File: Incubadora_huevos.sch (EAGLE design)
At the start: 53 parts, among them Q1 2N3904, Q2 2N3904, Q3 2N3904, T1 BT138-H, T2 BT138-H, T3 BT138-H, U1 SHT20

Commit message: Terminado ubicacion componentes. inicio ruteo
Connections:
- net LINEA: now also VAC-2.KL; no longer VAC-1.KL
- net NEUTR: now also VAC-1.KL; no longer VAC-2.KL
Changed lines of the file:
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@@
 <setting verticaltext="up"/>
 </settings>
-<grid distance="0.1" unitdist="inch" unit="inch" style="lines" multiple="1" display="yes" altdistance="0.01" altunitdist="inch" altunit="inch"/>
+<grid distance="0.1" unitdist="inch" unit="inch" style="lines" multiple="1" display="no" altdistance="0.01" altunitdist="inch" altunit="inch"/>
 <layers>
 <layer number="1" name="Top" color="4" fill="1" visible="no" active="no"/>
@@
 <net name="LINEA" class="0">
 <segment>
-<pinref part="VAC" gate="-1" pin="KL"/>
-<wire x1="60.96" y1="30.48" x2="63.5" y2="30.48" width="0.1524" layer="91"/>
-<label x="63.5" y="30.48" size="1.778" layer="95" ratio="10" xref="yes"/>
-</segment>
-<segment>
 <pinref part="R5" gate="G$1" pin="2"/>
 <pinref part="T1" gate="G$1" pin="A2"/>
@@
 <label x="147.32" y="114.3" size="1.778" layer="95" ratio="10" xref="yes"/>
 </segment>
-</net>
-<net name="NEUTR" class="0">
 <segment>
 <pinref part="VAC" gate="-2" pin="KL"/>
@@
 <label x="63.5" y="22.86" size="1.778" layer="95" ratio="10" xref="yes"/>
 </segment>
+</net>
+<net name="NEUTR" class="0">
 <segment>
 <pinref part="BOM1" gate="-2" pin="KL"/>
@@
 <wire x1="236.22" y1="78.74" x2="233.68" y2="78.74" width="0.1524" layer="91"/>
 <label x="233.68" y="78.74" size="1.778" layer="95" ratio="10" rot="R180" xref="yes"/>
+</segment>
+<segment>
+<pinref part="VAC" gate="-1" pin="KL"/>
+<wire x1="60.96" y1="30.48" x2="63.5" y2="30.48" width="0.1524" layer="91"/>
+<label x="63.5" y="30.48" size="1.778" layer="95" ratio="10" xref="yes"/>
 </segment>
 </net>
@@
 </sheet>
 </sheets>
+<errors>
+</errors>
 </schematic>
 </drawing>

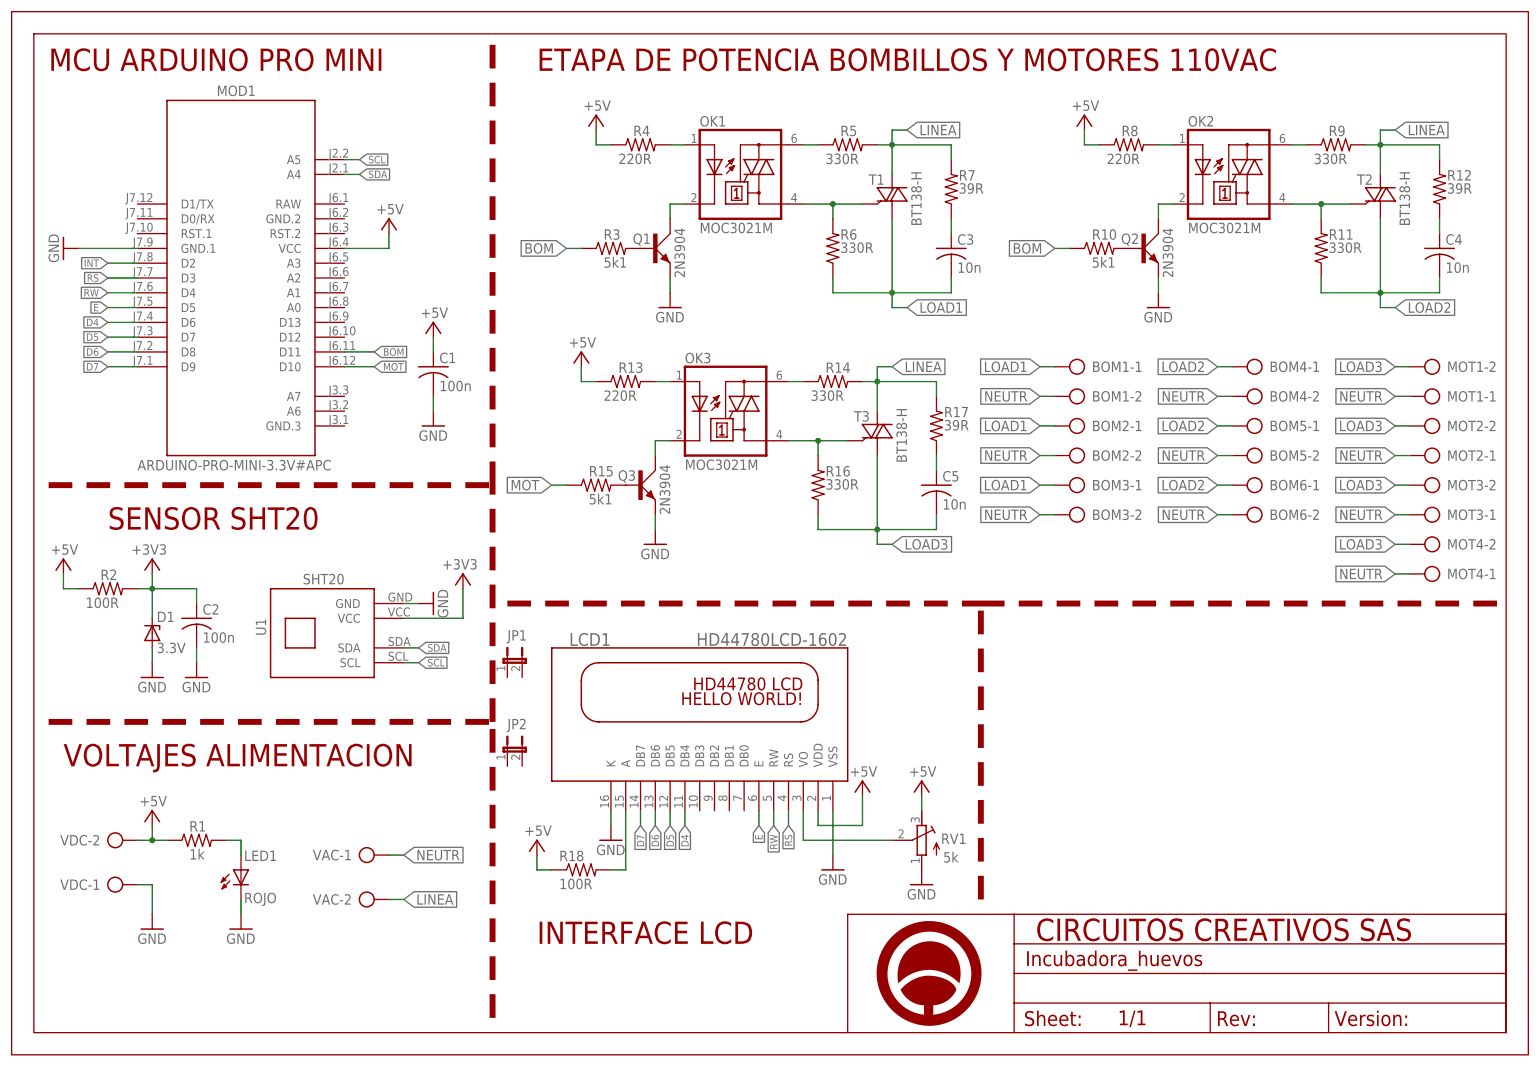
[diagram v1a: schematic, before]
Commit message: Se modifico la etapa de potencia ya que la anterior se calentaba mucho
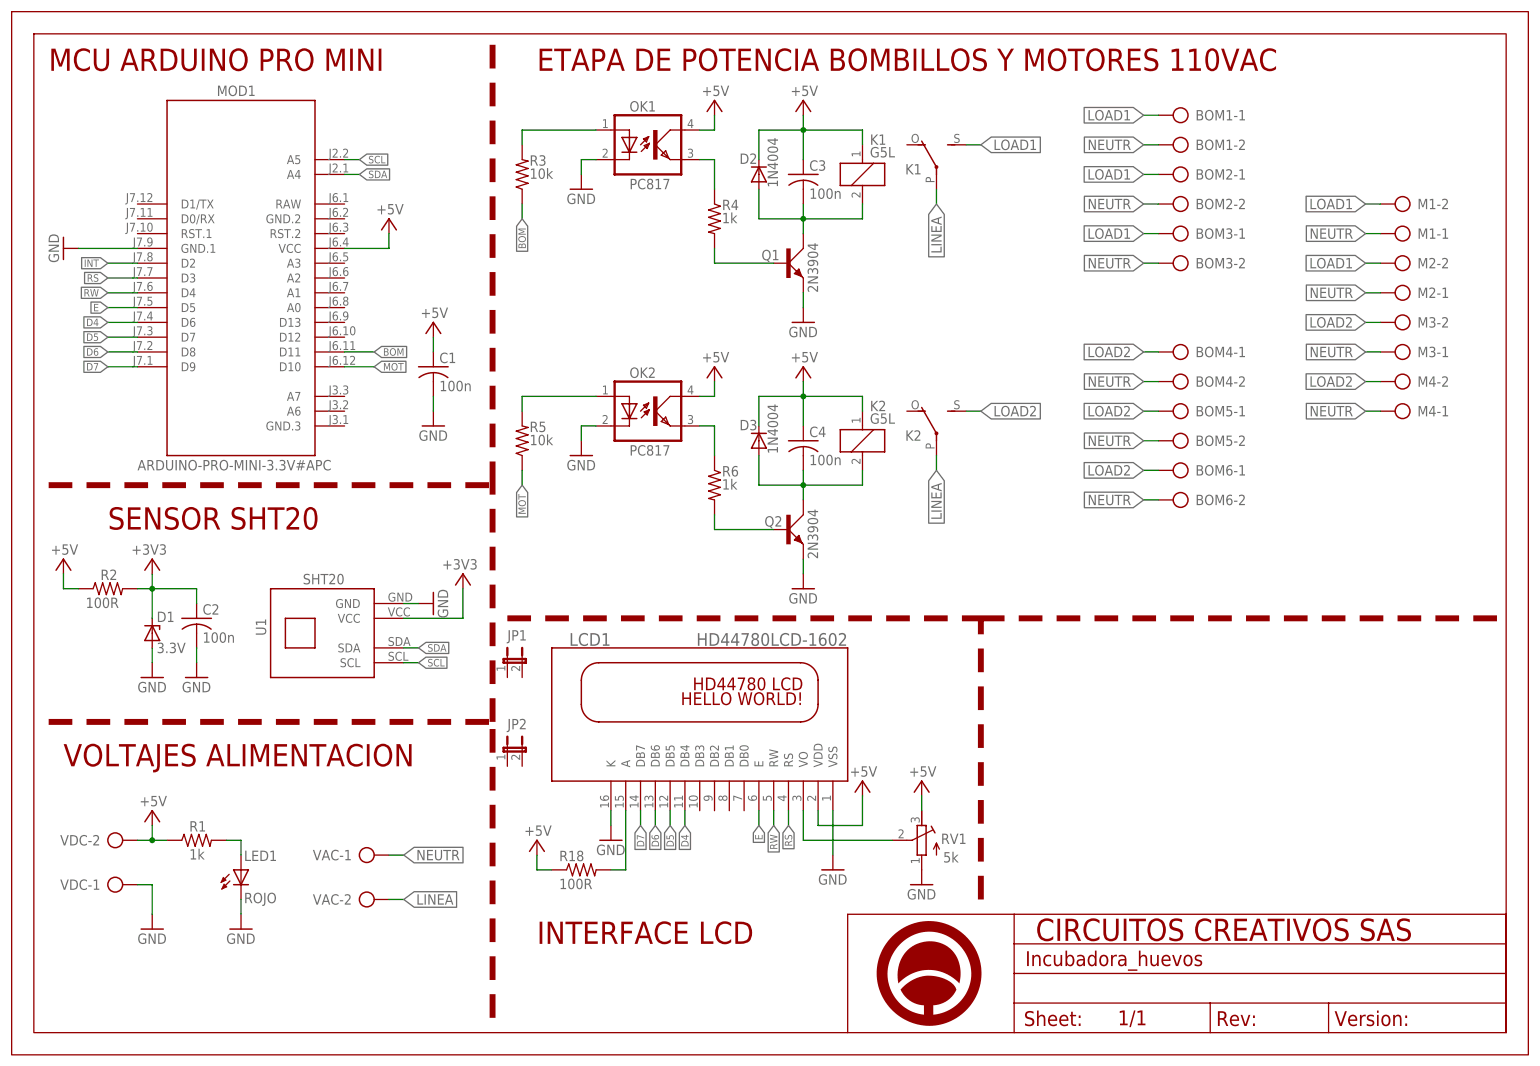
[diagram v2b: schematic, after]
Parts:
- removed C5: 10n, rcl:C-US050-030X075
- removed MOT1, MOT2, MOT3, MOT4: (no value), con-ptr500:AK500/2
- removed OK3: MOC3021M, optocoupler:MOC3021M
- removed Q3: 2N3904, transistor-small-signal:2N3904
- removed R10, R15: 5k1, rcl:R-US_0204/7
- removed R11, R14, R16, R9: 330R, rcl:R-US_0204/7
- removed R12, R17, R7: 39R, rcl:R-US_0204/7
- removed R13, R8: 220R, rcl:R-US_0204/7
- removed T1, T2, T3: BT138-H, triac:BT138-H
- added D2, D3: 1N4004, adafruit:1N4004
- added K1, K2: G5L, relay:G5L
- added M1, M2, M3, M4: (no value), con-ptr500:AK500/2
- C3, C4: value 10n -> 100n; device rcl:C-US050-030X075 -> rcl:C-US025-025X050
- OK1, OK2: value MOC3021M -> PC817; device optocoupler:MOC3021M -> optocoupler:PC817
- R3: value 5k1 -> 10k
- R4: value 220R -> 1k
- R5: value 330R -> 10k
- R6: value 330R -> 1k
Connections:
- removed net LOAD3: C5.2, MOT1-2.KL, MOT2-2.KL, MOT3-2.KL, MOT4-2.KL, R16.1, T3.A1
- removed net N$10: OK2.A2, R9.1
- removed net N$11: Q2.B, R10.2
- removed net N$12: OK2.C, Q2.C
- removed net N$13: C4.1, R12.1
- removed net N$14: OK3.A1, R16.2, T3.G
- removed net N$15: OK3.A, R13.2
- removed net N$16: OK3.A2, R14.1
- removed net N$17: Q3.B, R15.2
- removed net N$18: OK3.C, Q3.C
- removed net N$19: C5.1, R17.1
- removed net N$9: C3.1, R7.1
- new net N$21: C3.2, D2.A, K11.2, Q1.C
- net +5V: now also C3.1, C4.1, D2.C, D3.C, K11.1, K21.1, OK1.COL, OK2.COL; no longer R13.1, R4.1, R8.1
- net BOM: no longer R10.1
- net GND: now also OK1.C, OK2.C; no longer Q3.E
- net LINEA: now also K12.P, K22.P; no longer R12.2, R14.2, R17.2, R5.2, R7.2, R9.2, T1.A2, T2.A2, T3.A2
- net LOAD1: now also K12.S, M1-2.KL, M2-2.KL; no longer C3.2, R6.1, T1.A1
- net LOAD2: now also K22.S, M3-2.KL, M4-2.KL; no longer C4.2, R11.1, T2.A1
- net MOT: now also R5.1; no longer R15.1
- net N$2: now also OK1.EMIT, R4.1; no longer OK1.A1, R6.2, T1.G
- net N$3: now also Q1.B; no longer OK1.A
- net N$4: now also OK1.A, R3.2; no longer OK1.A2, R5.1
- net N$5: now also C4.2, D3.A, K21.2, Q2.C; no longer Q1.B, R3.2
- net N$6: now also OK2.EMIT, R6.1; no longer OK1.C, Q1.C
- net N$7: now also Q2.B, R6.2; no longer OK2.A1, R11.2, T2.G
- net N$8: now also R5.2; no longer R8.2
- net NEUTR: now also M1-1.KL, M2-1.KL, M3-1.KL, M4-1.KL; no longer MOT1-1.KL, MOT2-1.KL, MOT3-1.KL, MOT4-1.KL
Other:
- moved on the sheet: BOM1-1, BOM1-2, BOM2-1, BOM2-2, BOM3-1, BOM3-2, BOM4-1, BOM4-2, BOM5-1, BOM5-2, BOM6-1, BOM6-2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
